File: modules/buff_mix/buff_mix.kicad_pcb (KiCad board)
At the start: 2 copper layers, 27.9 x 66 mm, 2 parts

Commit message: Add the final buff_mix
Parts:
- added C1: C_Small, Capacitor_THT:C_Disc_D4.3mm_W1.9mm_P5.00mm, F.Cu at (50.8, 93.9)
- added C2: C_Small, Capacitor_THT:C_Disc_D4.3mm_W1.9mm_P5.00mm, F.Cu at (54.9, 78.7)
- added C3: C_Small, Capacitor_THT:C_Disc_D4.3mm_W1.9mm_P5.00mm, F.Cu at (69.8, 78.7)
- added C4: C_Small, Capacitor_THT:C_Disc_D4.3mm_W1.9mm_P5.00mm, F.Cu at (54.9, 68.5)
- added C5: C_Small, Capacitor_THT:C_Disc_D4.3mm_W1.9mm_P5.00mm, F.Cu at (73.7, 66.0)
- added INPUTS: Conn_01x05_Socket, Connector_PinSocket_2.54mm:PinSocket_1x05_P2.54mm_Vertical, F.Cu at (50.8, 45.7)
- added MIXOUT: Conn_01x05_Socket, Connector_PinSocket_2.54mm:PinSocket_1x05_P2.54mm_Vertical, F.Cu at (73.7, 45.7)
- added R1: 10K, Resistor_THT:R_Axial_DIN0207_L6.3mm_D2.5mm_P10.16mm_Horizontal, F.Cu at (63.5, 100.1)
- added R2: 10K, Resistor_THT:R_Axial_DIN0207_L6.3mm_D2.5mm_P10.16mm_Horizontal, F.Cu at (50.8, 100.1)
- added R3: 100K, Resistor_THT:R_Axial_DIN0207_L6.3mm_D2.5mm_P10.16mm_Horizontal, F.Cu at (71.1, 83.8)
- added R4: 100K, Resistor_THT:R_Axial_DIN0207_L6.3mm_D2.5mm_P10.16mm_Horizontal, F.Cu at (50.8, 86.4)
- added R5: 100K, Resistor_THT:R_Axial_DIN0207_L6.3mm_D2.5mm_P10.16mm_Horizontal, F.Cu at (50.8, 73.7)
- added R6: 100K, Resistor_THT:R_Axial_DIN0207_L6.3mm_D2.5mm_P10.16mm_Horizontal, F.Cu at (73.7, 78.7)
- added R7: 100K, Resistor_THT:R_Axial_DIN0207_L6.3mm_D2.5mm_P10.16mm_Horizontal, F.Cu at (57.4, 54.9)
- added R8: 100K, Resistor_THT:R_Axial_DIN0207_L6.3mm_D2.5mm_P10.16mm_Horizontal, F.Cu at (69.8, 70.6)
- added U1: LM358, Library:LM358_THT, F.Cu at (61.2, 88.9)
- added U2: LM358, Library:LM358_THT, F.Cu at (61.2, 76.2)
- added U3: LM358, Library:LM358_THT, F.Cu at (61.2, 62.7)
- moved 5V1 2.54 mm to (55.9, 50.8)
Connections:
- 5V1 pad 1: unconnected-(5V1-Pin_1-Pad1) -> +5V
- 5V1 pad 2: unconnected-(5V1-Pin_2-Pad2) -> +5V
- 5V1 pad 3: unconnected-(5V1-Pin_3-Pad3) -> +5V
- 5V1 pad 4: unconnected-(5V1-Pin_4-Pad4) -> +5V
- 5V1 pad 5: unconnected-(5V1-Pin_5-Pad5) -> +5V
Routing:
- net Net-(U1B--): track 0.00 -> 83.2 mm
- net +5V: track 0.00 -> 65.1 mm
- net INPUT 1: track 0.00 -> 64.6 mm
- net MIX OUT: track 0.00 -> 62.1 mm
- net INPUT 3: track 0.00 -> 54.0 mm
- net GND: track 10.2 -> 50.0 mm
- net INPUT 2: track 0.00 -> 31.9 mm
- net INPUT 5: track 0.00 -> 29.2 mm
- net INPUT 4: track 0.00 -> 18.4 mm
- net Net-(U1B-+): track 0.00 -> 16.7 mm
- net Net-(U1A--): track 0.00 -> 13.0 mm
- net Net-(C5-Pad2): track 0.00 -> 12.6 mm
- net Net-(U3A--): track 0.00 -> 11.6 mm
- net Net-(U3B--): track 0.00 -> 11.2 mm
- net Net-(C4-Pad2): track 0.00 -> 9.69 mm
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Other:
- board text added: "BUFF MIX"
- board text removed: "NAME"

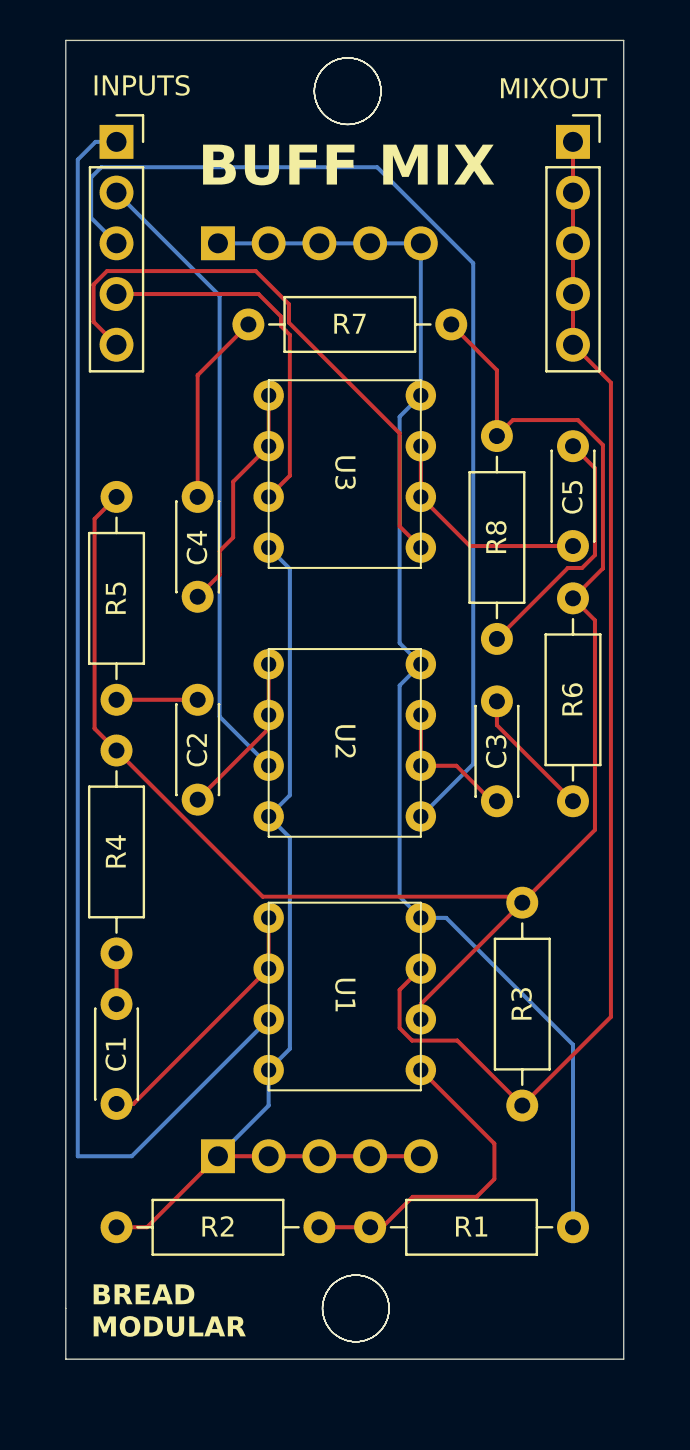
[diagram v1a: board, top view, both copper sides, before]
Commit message: Designed the new buff_mix 0.2.0 schematic.
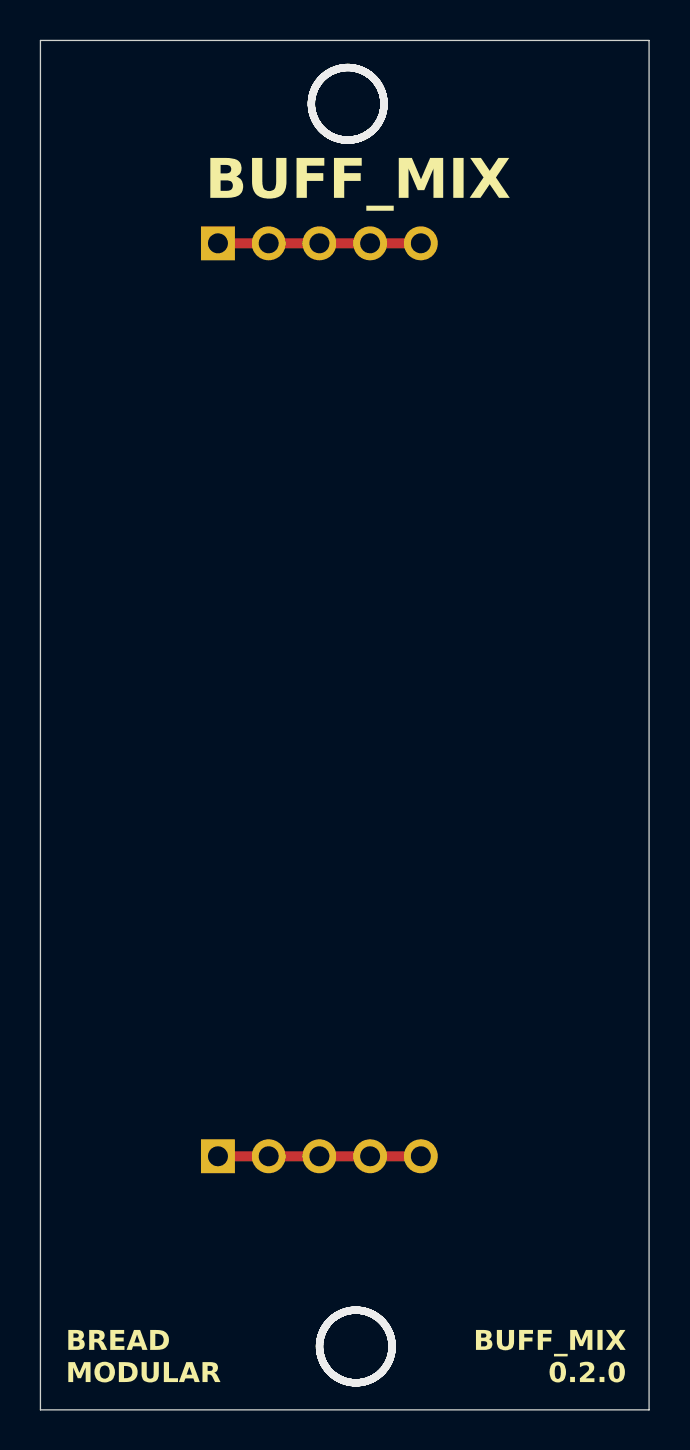
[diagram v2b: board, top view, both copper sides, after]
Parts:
- removed C1, C2, C3, C4, C5: C_Small, Capacitor_THT:C_Disc_D4.3mm_W1.9mm_P5.00mm
- removed INPUTS, MIXOUT: Conn_01x05_Socket, Connector_PinSocket_2.54mm:PinSocket_1x05_P2.54mm_Vertical
- removed R1, R2: 10K, Resistor_THT:R_Axial_DIN0207_L6.3mm_D2.5mm_P10.16mm_Horizontal
- removed R3, R4, R5, R6, R7, R8: 100K, Resistor_THT:R_Axial_DIN0207_L6.3mm_D2.5mm_P10.16mm_Horizontal
- removed U1, U2, U3: LM358, Library:LM358_THT
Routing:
- net Net-(U1B--): track 83.2 -> 0.00 mm
- net INPUT 1: track 64.6 -> 0.00 mm
- net MIX OUT: track 62.1 -> 0.00 mm
- net +5V: track 65.1 -> 10.2 mm
- net INPUT 3: track 54.0 -> 0.00 mm
- net GND: track 50.0 -> 10.2 mm
- net INPUT 2: track 31.9 -> 0.00 mm
- net INPUT 5: track 29.2 -> 0.00 mm
- net INPUT 4: track 18.4 -> 0.00 mm
- net Net-(U1B-+): track 16.7 -> 0.00 mm
- net Net-(U1A--): track 13.0 -> 0.00 mm
- net Net-(C5-Pad2): track 12.6 -> 0.00 mm
- net Net-(U3A--): track 11.6 -> 0.00 mm
- net Net-(U3B--): track 11.2 -> 0.00 mm
- net Net-(C4-Pad2): track 9.69 -> 0.00 mm
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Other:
- board size 27.9 x 66 mm -> 30.5 x 68.6 mm
- board text added: "BUFF_MIX"
- board text added: "BUFF_MIX 0.2.0"
- board text removed: "BUFF MIX"

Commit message: Add the PCB layout of buff_mix
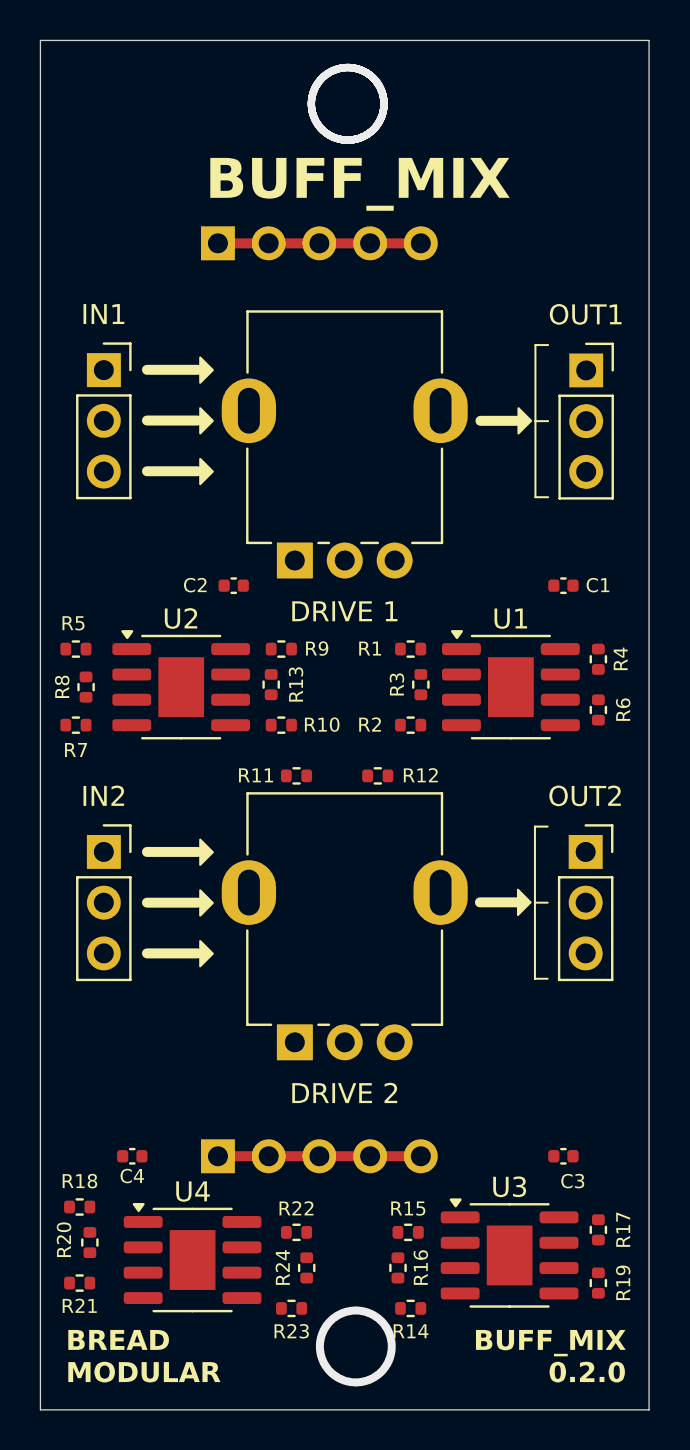
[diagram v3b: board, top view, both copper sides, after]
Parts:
- added C1: 0.1uf, Capacitor_SMD:C_0402_1005Metric, F.Cu at (73.2, 67.9)
- added C2: 0.1uf, Capacitor_SMD:C_0402_1005Metric, F.Cu at (56.7, 67.9)
- added C3: 0.1uf, Capacitor_SMD:C_0402_1005Metric, F.Cu at (73.2, 96.5)
- added C4: 0.1uf, Capacitor_SMD:C_0402_1005Metric, F.Cu at (51.6, 96.5)
- added IN1: Conn_01x03_Socket, Connector_PinSocket_2.54mm:PinSocket_1x03_P2.54mm_Vertical, F.Cu at (50.2, 57.1)
- added IN2: Conn_01x03_Socket, Connector_PinSocket_2.54mm:PinSocket_1x03_P2.54mm_Vertical, F.Cu at (50.2, 81.3)
- added OUT1: Conn_01x03_Socket, Connector_PinSocket_2.54mm:PinSocket_1x03_P2.54mm_Vertical, F.Cu at (74.3, 57.2)
- added OUT2: Conn_01x03_Socket, Connector_PinSocket_2.54mm:PinSocket_1x03_P2.54mm_Vertical, F.Cu at (74.3, 81.3)
- added R1: 1M, Resistor_SMD:R_0402_1005Metric, F.Cu at (65.5, 71.1)
- added R10: 1M, Resistor_SMD:R_0402_1005Metric, F.Cu at (59.1, 74.9)
- added R11: 1k, Resistor_SMD:R_0402_1005Metric, F.Cu at (59.8, 77.5)
- added R12: 1k, Resistor_SMD:R_0402_1005Metric, F.Cu at (63.9, 77.5)
- added R13: 1M, Resistor_SMD:R_0402_1005Metric, F.Cu at (58.5, 72.9)
- added R14: 1M, Resistor_SMD:R_0402_1005Metric, F.Cu at (65.5, 104.1)
- added R15: 1M, Resistor_SMD:R_0402_1005Metric, F.Cu at (65.4, 100.3)
- added R16: 1M, Resistor_SMD:R_0402_1005Metric, F.Cu at (64.9, 102.1)
- added R17: 1k, Resistor_SMD:R_0402_1005Metric, F.Cu at (74.9, 100.2)
- added R18: 1M, Resistor_SMD:R_0402_1005Metric, F.Cu at (49.0, 99.1)
- added R19: 1M, Resistor_SMD:R_0402_1005Metric, F.Cu at (74.9, 102.9)
- added R2: 1M, Resistor_SMD:R_0402_1005Metric, F.Cu at (65.5, 74.9)
- added R20: 1M, Resistor_SMD:R_0402_1005Metric, F.Cu at (49.5, 100.8)
- added R21: 1M, Resistor_SMD:R_0402_1005Metric, F.Cu at (49.0, 102.9)
- added R22: 1M, Resistor_SMD:R_0402_1005Metric, F.Cu at (59.8, 100.3)
- added R23: 1M, Resistor_SMD:R_0402_1005Metric, F.Cu at (59.6, 104.1)
- added R24: 1M, Resistor_SMD:R_0402_1005Metric, F.Cu at (60.3, 102.1)
- added R3: 1M, Resistor_SMD:R_0402_1005Metric, F.Cu at (66.0, 72.9)
- added R4: 1k, Resistor_SMD:R_0402_1005Metric, F.Cu at (74.9, 71.6)
- added R5: 1M, Resistor_SMD:R_0402_1005Metric, F.Cu at (48.8, 71.1)
- added R6: 1M, Resistor_SMD:R_0402_1005Metric, F.Cu at (74.9, 74.2)
- added R7: 1M, Resistor_SMD:R_0402_1005Metric, F.Cu at (48.8, 74.9)
- added R8: 1M, Resistor_SMD:R_0402_1005Metric, F.Cu at (49.3, 73.0)
- added R9: 1M, Resistor_SMD:R_0402_1005Metric, F.Cu at (59.1, 71.1)
- added RV1: 1M, BreadModular_Pots:Potentiometer_RV09, F.Cu at (59.7, 66.7)
- added RV2: 1M, BreadModular_Pots:Potentiometer_RV09, F.Cu at (59.7, 90.8)
- added U1: MCP6002-xSN, Package_SO:SOIC-8-1EP_3.9x4.9mm_P1.27mm_EP2.29x3mm, F.Cu at (70.5, 73.0)
- added U2: MCP6002-xSN, Package_SO:SOIC-8-1EP_3.9x4.9mm_P1.27mm_EP2.29x3mm, F.Cu at (54.0, 73.0)
- added U3: MCP6002-xSN, Package_SO:SOIC-8-1EP_3.9x4.9mm_P1.27mm_EP2.29x3mm, F.Cu at (70.5, 101.5)
- added U4: MCP6002-xSN, Package_SO:SOIC-8-1EP_3.9x4.9mm_P1.27mm_EP2.29x3mm, F.Cu at (54.6, 101.7)
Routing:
- net (no net): vias 8 -> 5
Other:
- board text added: "DRIVE 1"
- board text added: "DRIVE 2"

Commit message: Finished routing and production build
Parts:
- moved R14 3.82 mm to (65.3, 100.3)
- moved R15 3.81 mm to (65.3, 104.1)
- moved R20 2.08 mm to (49.0, 102.9), turned to 0 degrees
- moved R21 1.99 mm to (49.5, 101.0), turned to 90 degrees
- moved C4 1.91 mm to (51.6, 98.4)
- moved C2 1.50 mm to (55.9, 69.2)
- moved U4 0.41 mm to (54.6, 102.1)
- moved R16 0.18 mm to (64.8, 102.2), turned to 90 degrees
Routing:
- net +5V: track 10.2 -> 224.3 mm, vias 0 -> 5
- net +2.5V: track 0.00 -> 177.4 mm, vias 0 -> 9
- net GND: track 10.2 -> 181.3 mm, vias 0 -> 9
- net Net-(R14-Pad2): track 0.00 -> 63.1 mm, vias 0 -> 6
- net INB_1: track 0.00 -> 47.9 mm
- net INA_2: track 0.00 -> 37.9 mm
- net INA_1: track 0.00 -> 35.6 mm
- net Net-(R1-Pad2): track 0.00 -> 35.4 mm, vias 0 -> 4
- net INB_3: track 0.00 -> 28.3 mm
- net Net-(U3B--): track 0.00 -> 25.9 mm, vias 0 -> 2
- net Net-(U1B--): track 0.00 -> 23.7 mm, vias 0 -> 2
- net INA_3: track 0.00 -> 22.4 mm
- net INB_2: track 0.00 -> 20.3 mm
- net OUTB: track 0.00 -> 18.7 mm
- net OUTA: track 0.00 -> 15.3 mm
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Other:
- board text removed: "DRIVE 1"
